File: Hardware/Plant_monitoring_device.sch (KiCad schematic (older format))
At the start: 70 parts, among them J1 Barrel_Jack, J10 LED_PWM4, J11 SOIL1, J12 SOIL2, J13 SOIL3, J14 SOIL4, J2 SWO, J3 OUT1, J4 OUT2, J5 OUT3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

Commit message: Changes Step-down for LDO.
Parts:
- removed C35: 1uF, MRS_Passives:C0603, symbol MRS_Passives:C
- removed D31: CUS10F30, MRS_Diodes:SOD-323, symbol MRS_Diodes:Diode_Schottky
- removed L31: 4u7, MRS_Passives:L_DJNR3015, symbol MRS_Passives:L
- removed R31, R33: 10k, MRS_Passives:R0603, symbol MRS_Passives:R
- removed R32: 140k, MRS_Passives:R0603, symbol MRS_Passives:R
- removed U3: AOZ1282CI-1, MRS_SOT:SOT-23-6, symbol MRS_Power_Management:AOZ1282CI-1
- added U3: AP2204RB-3.3TRG1, MRS_SOT:SOT-89, symbol MRS_Power_Management:AP2204RB-3.3TRG1
- C33: value 0.1uF -> 10uF
- C34: value 10uF -> 1uF
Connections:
- wire segments 172 -> 160
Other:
- note removed: "Footprint"
- moved on the sheet: C31, C32

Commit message: Changes 2.54mm headers for 2mm connectors. Added a solderbridge to connect external supply with the mcu suply (so the outpust and pwms coul be used when the device is powered by a battery. Changed layout of the connectors. Made the PCB smaller.
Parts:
- removed J10: LED_PWM4, MRS_Connectors:Header_1x02_P2.54mm, symbol MRS_Connectors:Header_1x2
- removed J11: SOIL1, MRS_Connectors:Header_1x03_P2.54mm_Horizontal, symbol MRS_Connectors:Header_1x3
- removed J12: SOIL2, MRS_Connectors:Header_1x03_P2.54mm_Horizontal, symbol MRS_Connectors:Header_1x3
- removed J13: SOIL3, MRS_Connectors:Header_1x03_P2.54mm_Horizontal, symbol MRS_Connectors:Header_1x3
- removed J14: SOIL4, MRS_Connectors:Header_1x03_P2.54mm_Horizontal, symbol MRS_Connectors:Header_1x3
- removed J3: OUT1, MRS_Connectors:Header_1x02_P2.54mm, symbol MRS_Connectors:Header_1x2
- removed J4: OUT2, MRS_Connectors:Header_1x02_P2.54mm, symbol MRS_Connectors:Header_1x2
- removed J5: OUT3, MRS_Connectors:Header_1x02_P2.54mm, symbol MRS_Connectors:Header_1x2
- removed J6: OUT4, MRS_Connectors:Header_1x02_P2.54mm, symbol MRS_Connectors:Header_1x2
- removed J7: LED_PWM1, MRS_Connectors:Header_1x02_P2.54mm, symbol MRS_Connectors:Header_1x2
- removed J8: LED_PWM2, MRS_Connectors:Header_1x02_P2.54mm, symbol MRS_Connectors:Header_1x2
- removed J9: LED_PWM3, MRS_Connectors:Header_1x02_P2.54mm, symbol MRS_Connectors:Header_1x2
- added H2, H3: Mounting_hole_unplated_3,2mm, MRS_Mechanical:Mounting_hole_unplated_3,2mm, symbol MRS_Mechanical:Mounting_hole_unplated_3,2mm
- added J10, J3, J4, J5, J6, J7, J8, J9: NXW-02, MRS_Connectors:NXW-02, symbol MRS_Connectors:NXW-02
- added J11, J12, J13, J14: NXW-03, MRS_Connectors:NXW-03, symbol MRS_Connectors:NXW-03
- added SB2: SolderBridge, MRS_Connectors:SB0603, symbol MRS_Connectors:SolderBridge
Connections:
- net +12V: now also J10.1, J3.1, J4.1, J5.1, J6.1, J7.1, J8.1, J9.1, SB2.1
- net ADC_PH1: now also J11.2
- net ADC_PH2: now also J12.2
- net ADC_PH3: now also J13.2
- net ADC_PH4: now also J14.2
- net GND: now also J11.3, J12.3, J13.3, J14.3
- net VCC: now also SB2.2
- net VDDA: now also J11.1, J12.1, J13.1, J14.1
- net at Q7.3 (D): now also J7.2
- net at Q3.3 (D): now also J3.2
- net at Q4.3 (D): now also J4.2
- net at Q5.3 (D): now also J5.2
- net at Q6.3 (D): now also J6.2
- net at Q8.3 (D): now also J8.2
- net at Q9.3 (D): now also J9.2
- net at Q10.3 (D): now also J10.2

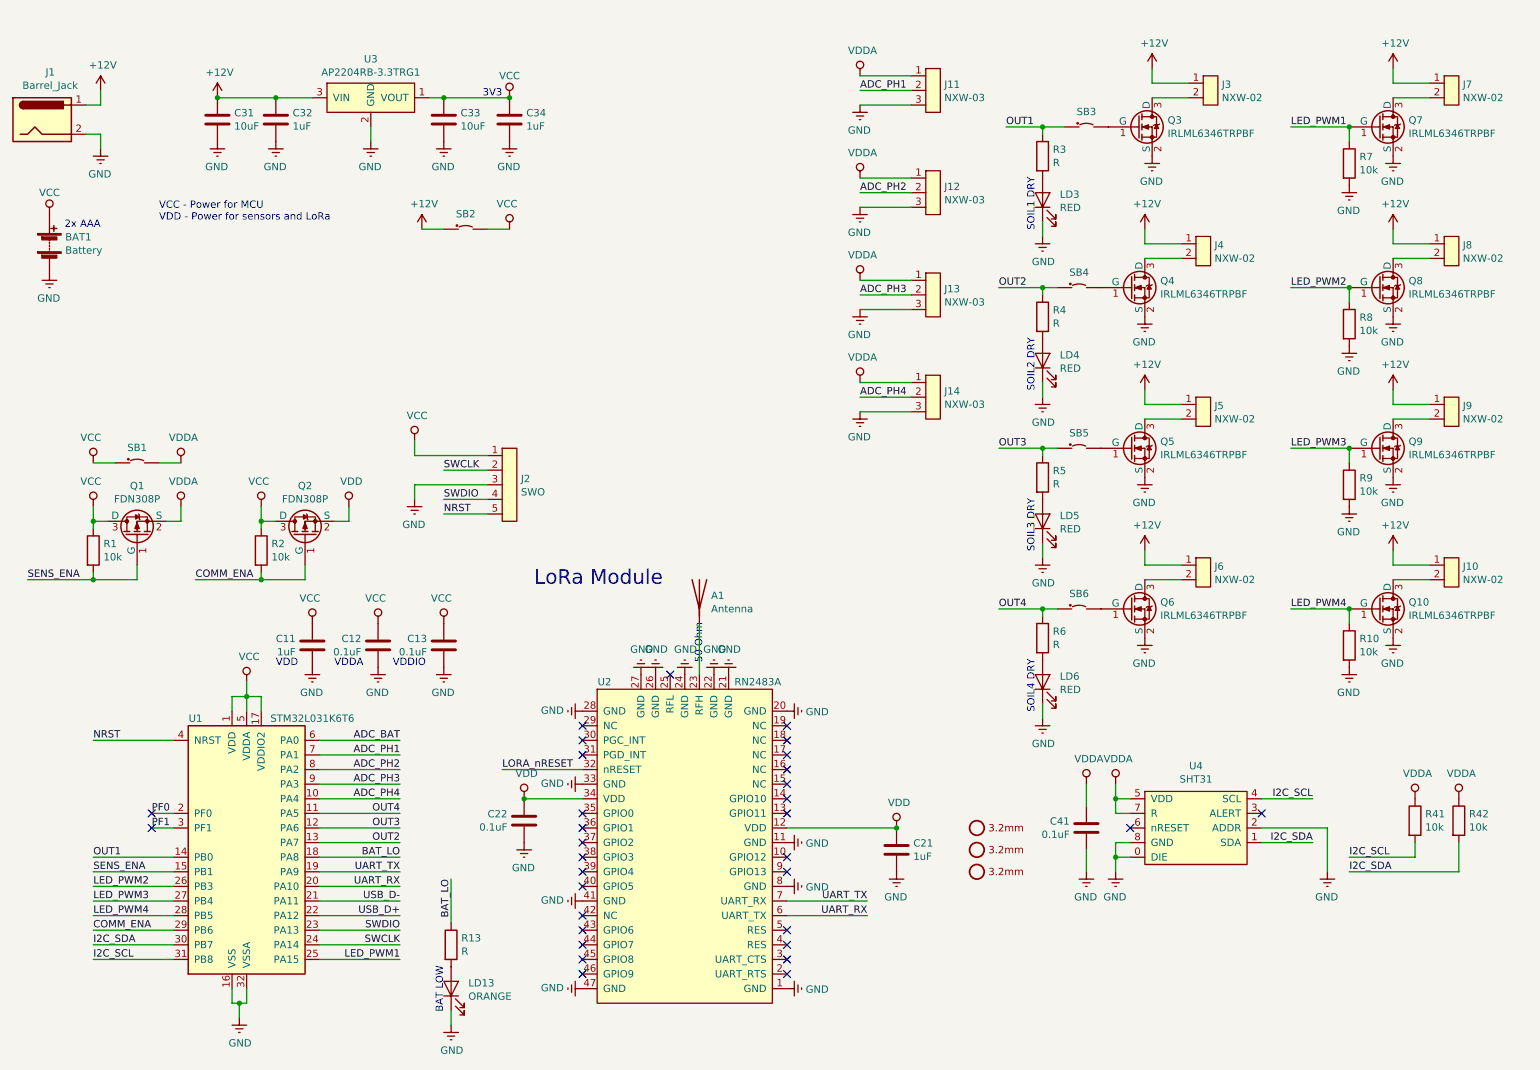
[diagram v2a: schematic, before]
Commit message: Swapped some pins to optmize track to tranzistors. Generated Gerbers.
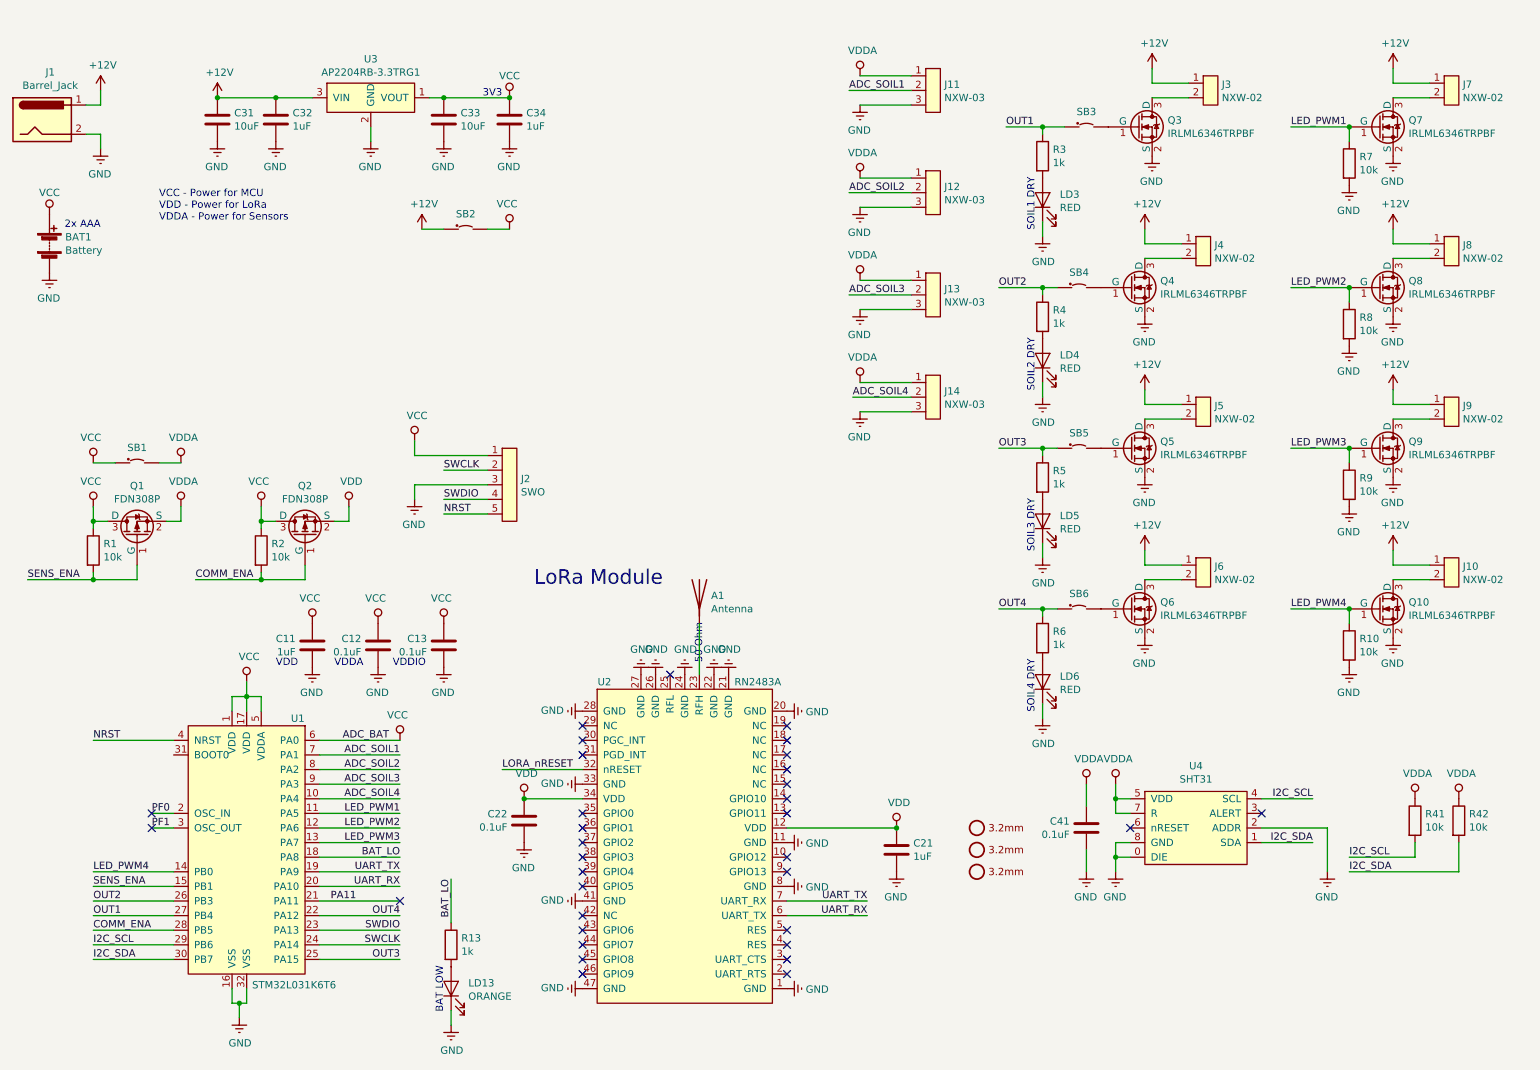
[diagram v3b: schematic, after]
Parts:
- removed U1: STM32L031K6T6, MRS_QFP:LQFP-32_7x7mm_P0.8mm, symbol MRS_MCUs:STM32F042K6T6
- added U1: STM32L031K6T6, MRS_QFP:LQFP-32_7x7mm_P0.8mm, symbol MRS_MCUs:STM32L031K6T6
- R13, R3, R4, R5, R6: value R -> 1k
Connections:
- net BAT_LO: now also U1.18 (PA8)
- net COMM_ENA: now also U1.28 (PB5)
- net GND: now also U1.16 (VSS), U1.32 (VSS)
- net I2C_SCL: now also U1.29 (PB6)
- net I2C_SDA: now also U1.30 (PB7)
- net LED_PWM1: now also U1.11 (PA5)
- net LED_PWM2: now also U1.12 (PA6)
- net LED_PWM3: now also U1.13 (PA7)
- net LED_PWM4: now also U1.14 (PB0)
- net NRST: now also U1.4 (NRST)
- net OUT1: now also U1.27 (PB4)
- net OUT2: now also U1.26 (PB3)
- net OUT3: now also U1.25 (PA15)
- net OUT4: now also U1.22 (PA12)
- net PF0: now also U1.2 (OSC_IN)
- net PF1: now also U1.3 (OSC_OUT)
- net SENS_ENA: now also U1.15 (PB1)
- net SWCLK: now also U1.24 (PA14)
- net SWDIO: now also U1.23 (PA13)
- net UART_RX: now also U1.20 (PA10)
- net UART_TX: now also U1.19 (PA9)
- net VCC: now also U1.1 (VDD), U1.17 (VDD), U1.5 (VDDA), U1.6 (PA0)
- net ADC_PH1 renamed ADC_SOIL1
- net ADC_SOIL1: now also U1.7 (PA1)
- net ADC_PH2 renamed ADC_SOIL2
- net ADC_SOIL2: now also U1.8 (PA2)
- net ADC_PH3 renamed ADC_SOIL3
- net ADC_SOIL3: now also U1.9 (PA3)
- net ADC_PH4 renamed ADC_SOIL4
- net ADC_SOIL4: now also U1.10 (PA4)
- new net PA11: U1.21 (PA11)
- no-connect marks 32 -> 33
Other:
- note added: "VCC - Power for MCU\nVDD - Power for LoRa\nVDDA - Power for Sensors"
- note removed: "VCC - Power for MCU\nVDD - Power for sensors and LoRa"
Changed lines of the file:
@@
 Comment4 ""
 $EndDescr
-$Comp
-L MRS_MCUs:STM32F042K6T6 U1
-U 1 1 5C9FAE86
-P 2300 6150
-F 0 "U1" H 1950 7100 50  0000 C CNN
-F 1 "STM32L031K6T6" H 2750 7100 50  0000 C CNN
-F 2 "MRS_QFP:LQFP-32_7x7mm_P0.8mm" H 1850 7000 50  0001 C CNN
-F 3 "https://www.tme.eu/Document/42c36ffe80e77edc307b35ead1f969f6/stm32l031k6.pdf" H 2300 5100 50  0001 C CNN
-F 4 "STM32L031K6T6" H 2300 5000 50  0001 C CNN "TME"
-	1    2300 6150
-	1    0    0    -1
-$EndComp
-Text Label 3350 5350 2    50   ~ 0
+Text Label 3275 5350 2    50   ~ 0
 ADC_BAT
 Text Label 3350 5450 2    50   ~ 0
-ADC_PH1
+ADC_SOIL1
 Text Label 3350 5550 2    50   ~ 0
-ADC_PH2
+ADC_SOIL2
 Text Label 3350 5650 2    50   ~ 0
-ADC_PH3
+ADC_SOIL3
 Text Label 3350 5750 2    50   ~ 0
-ADC_PH4
-Text Label 1250 6250 0    50   ~ 0
+ADC_SOIL4
+Text Label 1250 6350 0    50   ~ 0
 SENS_ENA
 Text Label 3350 6350 2    50   ~ 0
@@
 Text Label 3350 6250 2    50   ~ 0
 UART_TX
+Text Label 1250 6550 0    50   ~ 0
+OUT1
+Text Label 1250 6450 0    50   ~ 0
+OUT2
+Text Label 3350 6850 2    50   ~ 0
+OUT3
+Text Label 3350 6550 2    50   ~ 0
+OUT4
+Wire Wire Line
+	3350 5350 2800 5350
+Wire Wire Line
+	3350 5450 2800 5450
+Wire Wire Line
+	3350 5550 2800 5550
+Wire Wire Line
+	2800 5650 3350 5650
+Wire Wire Line
+	3350 5750 2800 5750
+Wire Wire Line
+	3350 5850 2800 5850
+Wire Wire Line
+	3350 5950 2800 5950
+Wire Wire Line
+	3350 6050 2800 6050
+Wire Wire Line
+	1800 6250 1250 6250
+Wire Wire Line
+	3350 6250 2800 6250
+Wire Wire Line
+	3350 6350 2800 6350
+Wire Wire Line
+	3350 6550 2800 6550
+Wire Wire Line
+	3350 6450 2800 6450
+Wire Wire Line
+	1800 6350 1250 6350
+Wire Wire Line
+	1800 6450 1250 6450
+Wire Wire Line
+	1800 6550 1250 6550
+Wire Wire Line
+	3350 6850 2800 6850
+Text Label 1250 6250 0    50   ~ 0
+LED_PWM4
+Text Label 3350 5950 2    50   ~ 0
+LED_PWM2
+Text Label 3350 6050 2    50   ~ 0
+LED_PWM3
 Text Label 3350 5850 2    50   ~ 0
-OUT4
-Text Label 3350 5950 2    50   ~ 0
-OUT3
-Text Label 3350 6050 2    50   ~ 0
-OUT2
-Text Label 1250 6150 0    50   ~ 0
-OUT1
-Wire Wire Line
-	3350 5350 2800 5350
-Wire Wire Line
-	3350 5450 2800 5450
-Wire Wire Line
-	3350 5550 2800 5550
-Wire Wire Line
-	2800 5650 3350 5650
-Wire Wire Line
-	3350 5750 2800 5750
-Wire Wire Line
-	3350 5850 2800 5850
-Wire Wire Line
-	3350 5950 2800 5950
-Wire Wire Line
-	3350 6050 2800 6050
-Wire Wire Line
-	1800 6150 1250 6150
-Wire Wire Line
-	1800 6250 1250 6250
-Wire Wire Line
-	3350 6250 2800 6250
-Wire Wire Line
-	3350 6350 2800 6350
-Wire Wire Line
-	3350 6550 2800 6550
-Wire Wire Line
-	3350 6450 2800 6450
-Text Label 3350 6450 2    50   ~ 0
-USB_D-
-Text Label 3350 6550 2    50   ~ 0
-USB_D+
-Wire Wire Line
-	1800 6350 1250 6350
-Wire Wire Line
-	1800 6450 1250 6450
-Wire Wire Line
-	1800 6550 1250 6550
-Wire Wire Line
-	3350 6850 2800 6850
-Text Label 3350 6850 2    50   ~ 0
 LED_PWM1
-Text Label 1250 6350 0    50   ~ 0
-LED_PWM2
-Text Label 1250 6450 0    50   ~ 0
-LED_PWM3
-Text Label 1250 6550 0    50   ~ 0
-LED_PWM4
+Text Label 1250 6850 0    50   ~ 0
+I2C_SDA
 Text Label 1250 6750 0    50   ~ 0
-I2C_SDA
-Text Label 1250 6850 0    50   ~ 0
 I2C_SCL
 Text Label 1650 5850 0    50   ~ 0
@@
 P 7750 1350
 F 0 "R3" H 7820 1396 50  0000 L CNN
-F 1 "R" H 7820 1305 50  0000 L CNN
+F 1 "1k" H 7820 1305 50  0000 L CNN
 F 2 "MRS_Passives:R0603" V 8150 1350 50  0001 C CNN
 F 3 "" V 7830 1350 50  0001 C CNN
@@
 P 7750 2450
 F 0 "R4" H 7820 2496 50  0000 L CNN
-F 1 "R" H 7820 2405 50  0000 L CNN
+F 1 "1k" H 7820 2405 50  0000 L CNN
 F 2 "MRS_Passives:R0603" V 8150 2450 50  0001 C CNN
 F 3 "" V 7830 2450 50  0001 C CNN
@@
 P 7750 3550
 F 0 "R5" H 7820 3596 50  0000 L CNN
-F 1 "R" H 7820 3505 50  0000 L CNN
+F 1 "1k" H 7820 3505 50  0000 L CNN
 F 2 "MRS_Passives:R0603" V 8150 3550 50  0001 C CNN
 F 3 "" V 7830 3550 50  0001 C CNN
@@
 P 7750 4650
 F 0 "R6" H 7820 4696 50  0000 L CNN
-F 1 "R" H 7820 4605 50  0000 L CNN
+F 1 "1k" H 7820 4605 50  0000 L CNN
 F 2 "MRS_Passives:R0603" V 8150 4650 50  0001 C CNN
 F 3 "" V 7830 4650 50  0001 C CNN
@@
 P 3700 6750
 F 0 "R13" H 3770 6796 50  0000 L CNN
-F 1 "R" H 3770 6705 50  0000 L CNN
+F 1 "1k" H 3770 6705 50  0000 L CNN
 F 2 "MRS_Passives:R0603" V 4100 6750 50  0001 C CNN
 F 3 "" V 3780 6750 50  0001 C CNN
@@
 $EndComp
 Text Notes 1700 1800 0    50   ~ 0
-VCC - Power for MCU\nVDD - Power for sensors and LoRa
+VCC - Power for MCU\nVDD - Power for LoRa\nVDDA - Power for Sensors
 Text Label 800  4250 0    50   ~ 0
 SENS_ENA
@@
 	-1   0    0    -1
 $EndComp
-Text Label 6500 900  0    50   ~ 0
-ADC_PH1
-Wire Wire Line
-	6500 900  6850 900
+Text Label 6425 900  0    50   ~ 0
+ADC_SOIL1
 Wire Wire Line
 	6850 1000 6500 1000
@@
 	-1   0    0    -1
 $EndComp
-Text Label 6500 1600 0    50   ~ 0
-ADC_PH2
-Wire Wire Line
-	6500 1600 6850 1600
+Text Label 6425 1600 0    50   ~ 0
+ADC_SOIL2
 Wire Wire Line
 	6850 1700 6500 1700
@@
 	-1   0    0    -1
 $EndComp
-Text Label 6500 2300 0    50   ~ 0
-ADC_PH3
-Wire Wire Line
-	6500 2300 6850 2300
+Text Label 6425 2300 0    50   ~ 0
+ADC_SOIL3
 Wire Wire Line
 	6850 2400 6500 2400
@@
 	-1   0    0    -1
 $EndComp
-Text Label 6500 3000 0    50   ~ 0
-ADC_PH4
-Wire Wire Line
-	6500 3000 6850 3000
+Text Label 6450 3000 0    50   ~ 0
+ADC_SOIL4
 Wire Wire Line
 	6850 3100 6500 3100
@@
 Wire Wire Line
 	2800 6650 3350 6650
-Wire Wire Line
-	2800 6750 3350 6750
 Text Label 3650 3700 0    50   ~ 0
 SWDIO
@@
 	1    0    0    -1
 $EndComp
+$Comp
+L MRS_MCUs:STM32L031K6T6 U1
+U 1 1 5CAFA03F
+P 2300 6150
+F 0 "U1" H 2650 7100 50  0000 C CNN
+F 1 "STM32L031K6T6" H 2625 5275 50  0000 C CNN
+F 2 "MRS_QFP:LQFP-32_7x7mm_P0.8mm" H 2300 5150 50  0001 C CNN
+F 3 "https://www.tme.eu/Document/42c36ffe80e77edc307b35ead1f969f6/stm32l031k6.pdf" H 2300 5050 50  0001 C CNN
+F 4 "STM32L031K6T6" H 2300 4950 50  0001 C CNN "TME"
+	1    2300 6150
+	1    0    0    -1
+$EndComp
+NoConn ~ 3350 6450
+Text Label 2875 6450 0    50   ~ 0
+PA11
+Wire Wire Line
+	6425 900  6850 900
+Wire Wire Line
+	6425 1600 6850 1600
+Wire Wire Line
+	6425 2300 6850 2300
+Wire Wire Line
+	6450 3000 6850 3000
+Wire Wire Line
+	3350 6750 2800 6750
+$Comp
+L MRS_Power:VCC #PWR0107
+U 1 1 5CB44371
+P 3350 5350
+F 0 "#PWR0107" H 3350 5200 50  0001 C CNN
+F 1 "VCC" H 3367 5523 50  0000 C CNN
+F 2 "" H 3350 5350 50  0001 C CNN
+F 3 "" H 3350 5350 50  0001 C CNN
+	1    3350 5350
+	-1   0    0    -1
+$EndComp
 $EndSCHEMATC
